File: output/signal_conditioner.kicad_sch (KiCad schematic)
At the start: 0 parts

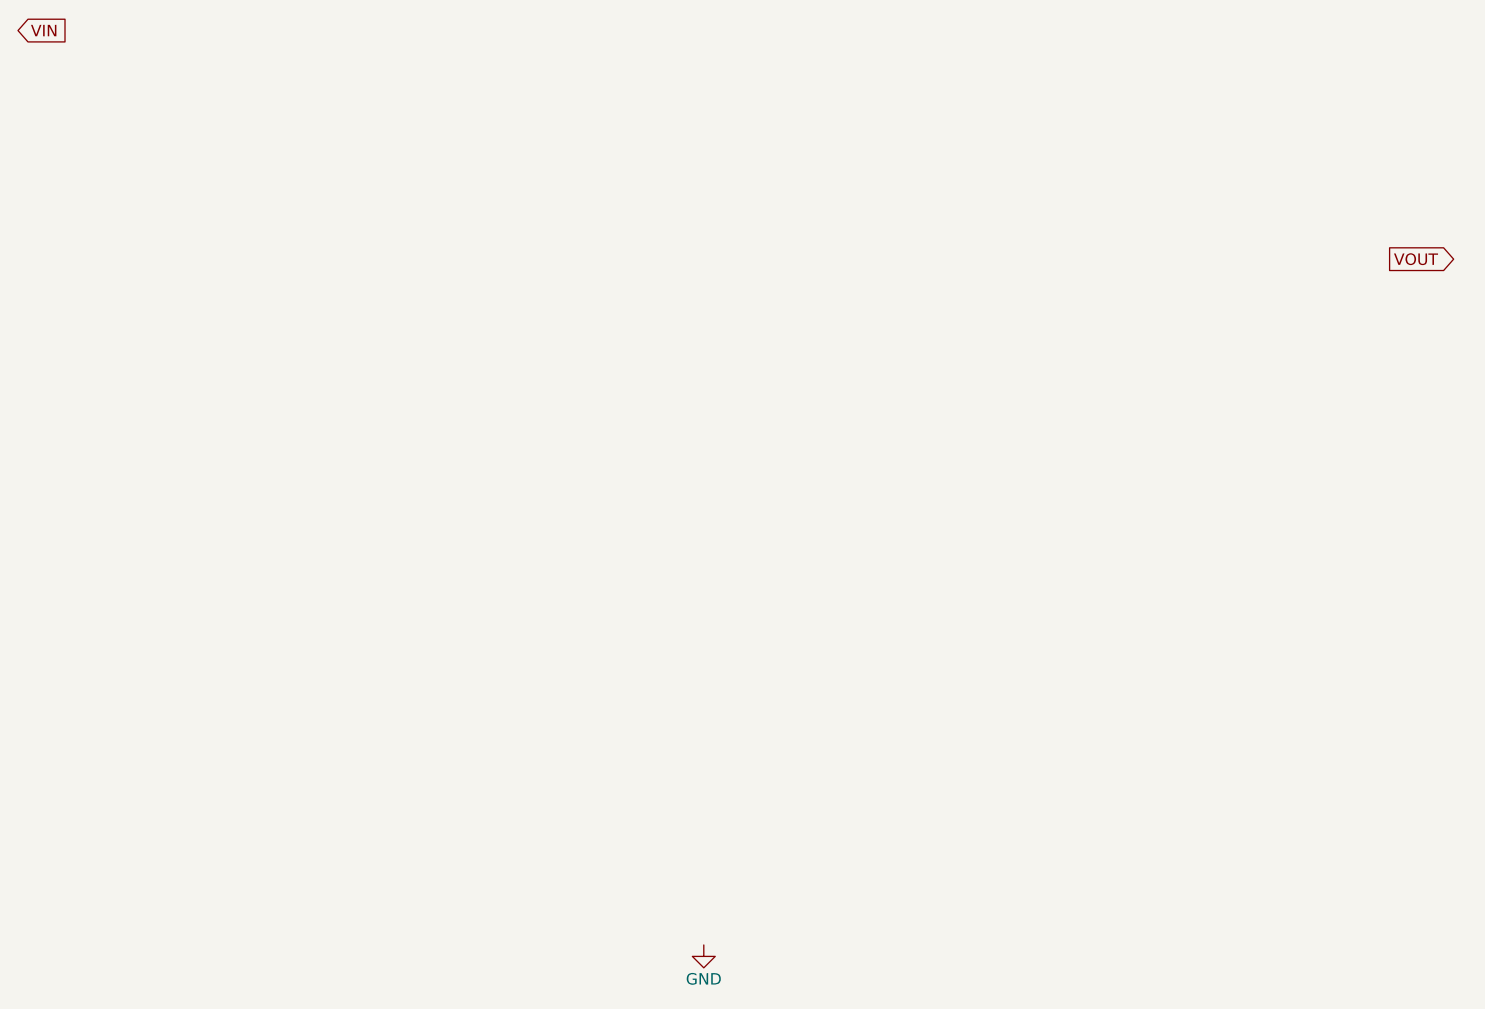
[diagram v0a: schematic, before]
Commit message: refactor: change placement engine, kicad_gen.py, add spring based layout
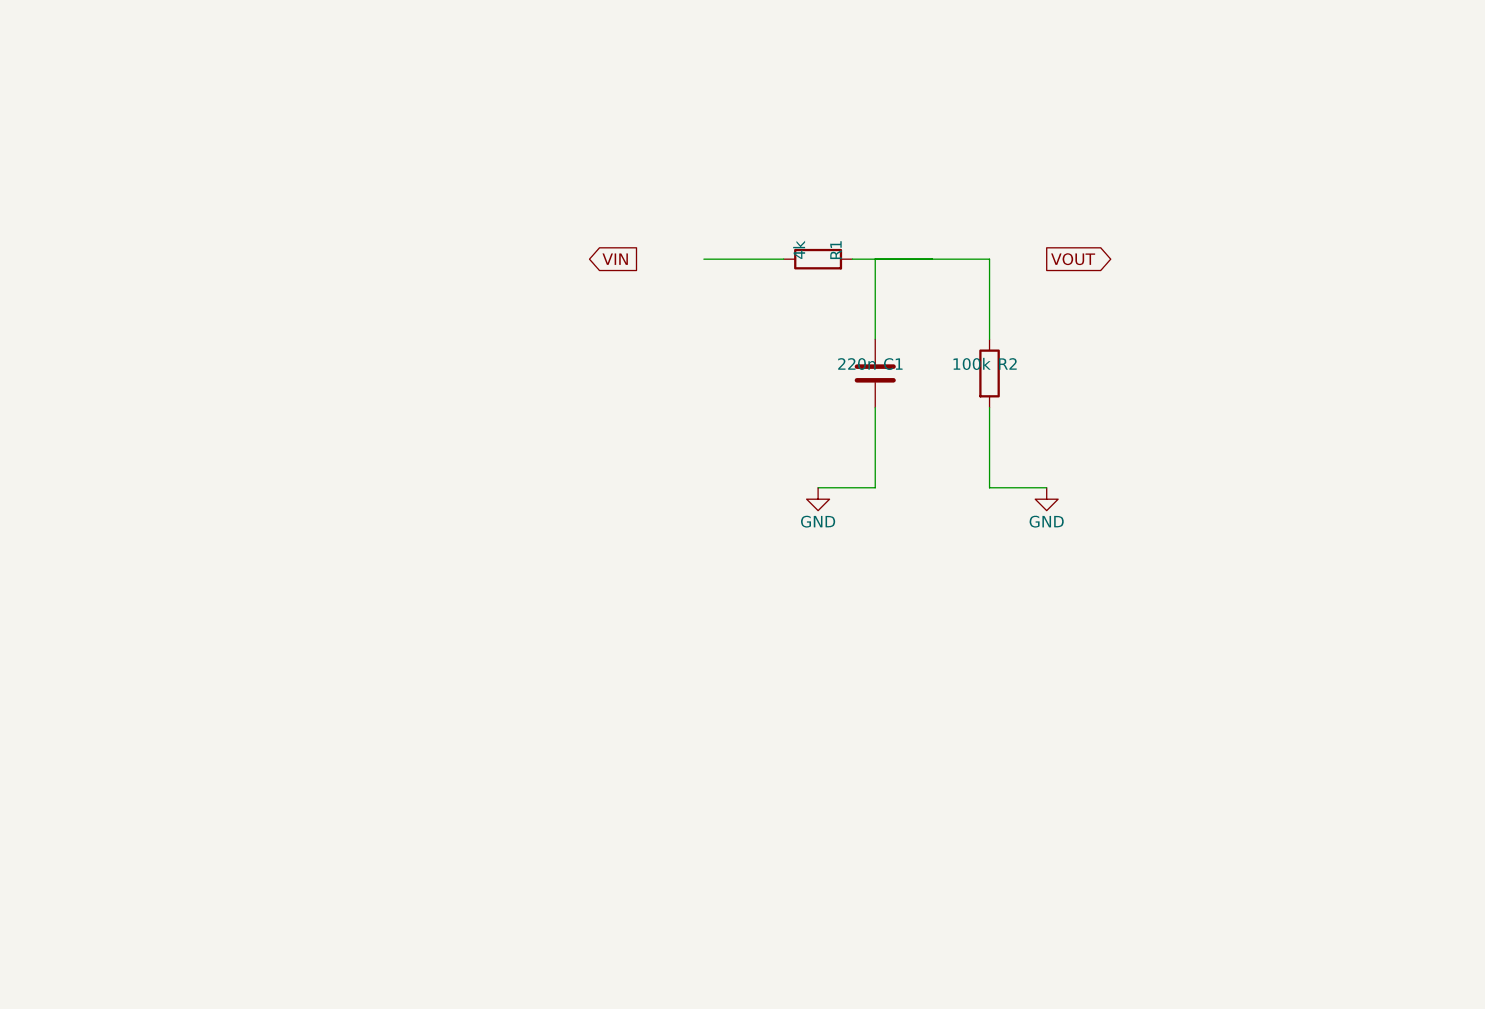
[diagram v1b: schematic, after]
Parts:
- added C1: 220n, symbol Device:C
- added R1: 4k, symbol Device:R
- added R2: 100k, symbol Device:R
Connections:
- net GND: now also C1.2, R2.2
- new net: C1.1, R1.2, R2.1
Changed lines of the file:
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@@
   (title_block (title "signal_conditioner"))
   (symbol
+    (lib_id "Device:R")
+    (at 162.7 100.0 90)
+    (unit 1)
+    (in_bom yes)
+    (on_board yes)
+    (property "Reference" "R1"
+      (at 164.732 99.0 0)
+      (effects (font (size 1.27 1.27)))
+    )
+    (property "Value" "4k"
+      (at 160.668 99.0 0)
+      (effects (font (size 1.27 1.27)))
+    )
+    (property "Footprint" "" (at 0 0 0)
+      (effects (font (size 1.27 1.27)) hide)
+    )
+    (property "Datasheet" "~" (at 0 0 0)
+      (effects (font (size 1.27 1.27)) hide)
+    )
+    (instances
+      (project "schematic"
+        (path "/df601bb8-62e9-4963-aebd-6cc9d662ebfd"
+          (reference "R1")
+          (unit 1)
+        )
+      )
+    )
+  )
+  (symbol
+    (lib_id "Device:C")
+    (at 169.05 112.7 0)
+    (unit 1)
+    (in_bom yes)
+    (on_board yes)
+    (property "Reference" "C1"
+      (at 171.082 111.7 0)
+      (effects (font (size 1.27 1.27)))
+    )
+    (property "Value" "220n"
+      (at 167.018 111.7 0)
+      (effects (font (size 1.27 1.27)))
+    )
+    (property "Footprint" "" (at 0 0 0)
+      (effects (font (size 1.27 1.27)) hide)
+    )
+    (property "Datasheet" "~" (at 0 0 0)
+      (effects (font (size 1.27 1.27)) hide)
+    )
+    (instances
+      (project "schematic"
+        (path "/df601bb8-62e9-4963-aebd-6cc9d662ebfd"
+          (reference "C1")
+          (unit 1)
+        )
+      )
+    )
+  )
+  (symbol
+    (lib_id "Device:R")
+    (at 181.75 112.7 0)
+    (unit 1)
+    (in_bom yes)
+    (on_board yes)
+    (property "Reference" "R2"
+      (at 183.782 111.7 0)
+      (effects (font (size 1.27 1.27)))
+    )
+    (property "Value" "100k"
+      (at 179.718 111.7 0)
+      (effects (font (size 1.27 1.27)))
+    )
+    (property "Footprint" "" (at 0 0 0)
+      (effects (font (size 1.27 1.27)) hide)
+    )
+    (property "Datasheet" "~" (at 0 0 0)
+      (effects (font (size 1.27 1.27)) hide)
+    )
+    (instances
+      (project "schematic"
+        (path "/df601bb8-62e9-4963-aebd-6cc9d662ebfd"
+          (reference "R2")
+          (unit 1)
+        )
+      )
+    )
+  )
+  (symbol
     (lib_id "power:GND")
-    (at 150.0 176.2 0)
+    (at 162.7 125.4 0)
     (unit 1)
     (in_bom yes)
     (on_board yes)
     (property "Reference" "#PWR01"
-      (at 150.0 182.55 0)
+      (at 162.7 131.75 0)
       (effects (font (size 1.27 1.27)) hide)
     )
     (property "Value" "GND"
-      (at 150.0 180.01 0)
+      (at 162.7 129.21 0)
       (effects (font (size 1.27 1.27)))
     )
@@
     (instances
       (project "schematic"
-        (path "/a8abd283-8ac3-43ae-b32d-a124fc3d4de3"
+        (path "/df601bb8-62e9-4963-aebd-6cc9d662ebfd"
           (reference "#PWR01")
+          (unit 1)
+        )
+      )
+    )
+  )
+  (symbol
+    (lib_id "power:GND")
+    (at 188.1 125.4 0)
+    (unit 1)
+    (in_bom yes)
+    (on_board yes)
+    (property "Reference" "#PWR02"
+      (at 188.1 131.75 0)
+      (effects (font (size 1.27 1.27)) hide)
+    )
+    (property "Value" "GND"
+      (at 188.1 129.21 0)
+      (effects (font (size 1.27 1.27)))
+    )
+    (property "Footprint" "" (at 0 0 0)
+      (effects (font (size 1.27 1.27)) hide)
+    )
+    (property "Datasheet" "" (at 0 0 0)
+      (effects (font (size 1.27 1.27)) hide)
+    )
+    (instances
+      (project "schematic"
+        (path "/df601bb8-62e9-4963-aebd-6cc9d662ebfd"
+          (reference "#PWR02")
           (unit 1)
         )
@@
   (global_label "VIN"
     (shape input)
-    (at 73.8 74.6 0)
+    (at 137.3 100.0 0)
     (fields_autoplaced yes)
     (effects (font (size 1.27 1.27)))
@@
   (global_label "VOUT"
     (shape output)
-    (at 226.2 100.0 0)
+    (at 188.1 100.0 0)
     (fields_autoplaced yes)
     (effects (font (size 1.27 1.27)))
@@
     )
   )
+  (wire
+    (pts (xy 150.0 100.0) (xy 158.89 100.0))
+    (stroke (width 0) (type default))
+  )
+  (wire
+    (pts (xy 175.4 100.0) (xy 166.51 100.0))
+    (stroke (width 0) (type default))
+  )
+  (wire
+    (pts (xy 175.4 100.0) (xy 169.05 100.0))
+    (stroke (width 0) (type default))
+  )
+  (wire
+    (pts (xy 169.05 100.0) (xy 169.05 108.89))
+    (stroke (width 0) (type default))
+  )
+  (wire
+    (pts (xy 162.7 125.4) (xy 169.05 125.4))
+    (stroke (width 0) (type default))
+  )
+  (wire
+    (pts (xy 169.05 125.4) (xy 169.05 116.51))
+    (stroke (width 0) (type default))
+  )
+  (wire
+    (pts (xy 175.4 100.0) (xy 181.75 100.0))
+    (stroke (width 0) (type default))
+  )
+  (wire
+    (pts (xy 181.75 100.0) (xy 181.75 108.89))
+    (stroke (width 0) (type default))
+  )
+  (wire
+    (pts (xy 188.1 125.4) (xy 181.75 125.4))
+    (stroke (width 0) (type default))
+  )
+  (wire
+    (pts (xy 181.75 125.4) (xy 181.75 116.51))
+    (stroke (width 0) (type default))
+  )
   (sheet_instances

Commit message: feat: revise pipeline
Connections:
- net VIN: now also R1.1
- net VOUT: now also C1.1, R1.2, R2.1
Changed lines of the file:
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@@
     (instances
       (project "schematic"
-        (path "/df601bb8-62e9-4963-aebd-6cc9d662ebfd"
+        (path "/1d0e848e-ee1b-4645-9321-6a5002ce66ca"
           (reference "R1")
           (unit 1)
@@
     (instances
       (project "schematic"
-        (path "/df601bb8-62e9-4963-aebd-6cc9d662ebfd"
+        (path "/1d0e848e-ee1b-4645-9321-6a5002ce66ca"
           (reference "C1")
           (unit 1)
@@
     (instances
       (project "schematic"
-        (path "/df601bb8-62e9-4963-aebd-6cc9d662ebfd"
+        (path "/1d0e848e-ee1b-4645-9321-6a5002ce66ca"
           (reference "R2")
           (unit 1)
@@
     (instances
       (project "schematic"
-        (path "/df601bb8-62e9-4963-aebd-6cc9d662ebfd"
+        (path "/1d0e848e-ee1b-4645-9321-6a5002ce66ca"
           (reference "#PWR01")
           (unit 1)
@@
     (instances
       (project "schematic"
-        (path "/df601bb8-62e9-4963-aebd-6cc9d662ebfd"
+        (path "/1d0e848e-ee1b-4645-9321-6a5002ce66ca"
           (reference "#PWR02")
           (unit 1)
@@
   (global_label "VIN"
     (shape input)
-    (at 137.3 100.0 0)
+    (at 140.0 100.0 0)
     (fields_autoplaced yes)
     (effects (font (size 1.27 1.27)))
@@
   (global_label "VOUT"
     (shape output)
-    (at 188.1 100.0 0)
+    (at 185.4 100.0 180)
     (fields_autoplaced yes)
     (effects (font (size 1.27 1.27)))
@@
     (stroke (width 0) (type default))
   )
+  (wire
+    (pts (xy 140.0 100.0) (xy 150.0 100.0))
+    (stroke (width 0) (type default))
+  )
+  (wire
+    (pts (xy 175.4 100.0) (xy 185.4 100.0))
+    (stroke (width 0) (type default))
+  )
